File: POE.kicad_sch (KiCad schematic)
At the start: 36 parts, among them J3 7466003R, J5 7466003R, Q1 FDS2582, T1 PA2369NL, U13 VO615A, U14 TL431PK, U3 NCP1081

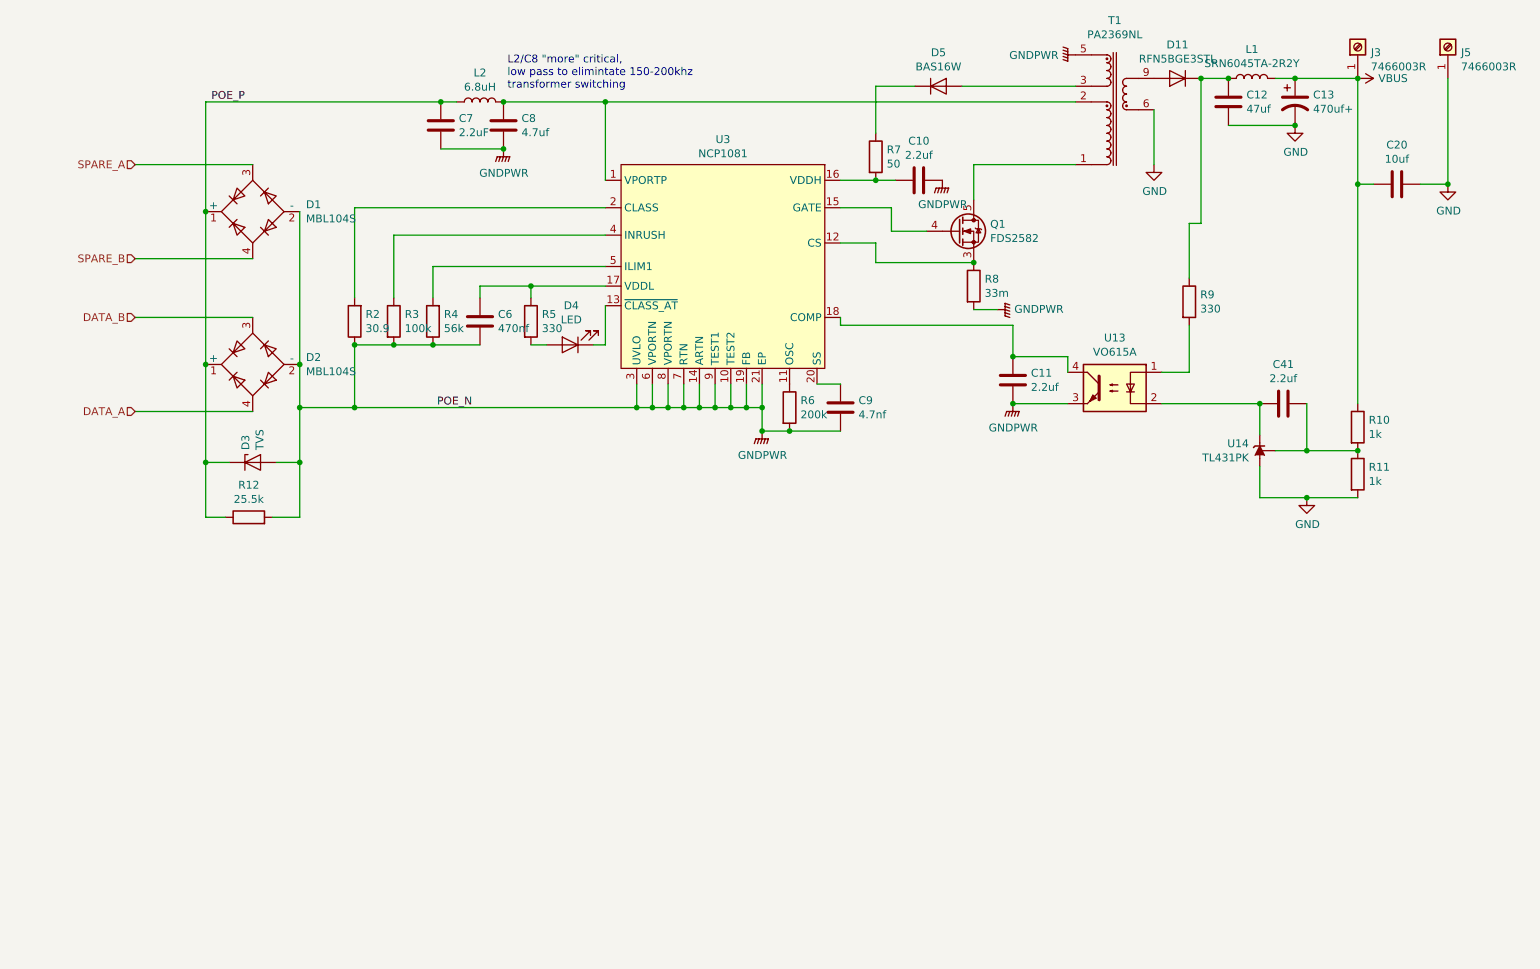
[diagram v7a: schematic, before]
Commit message: Swap low voltage caps, remove hv side LC filter
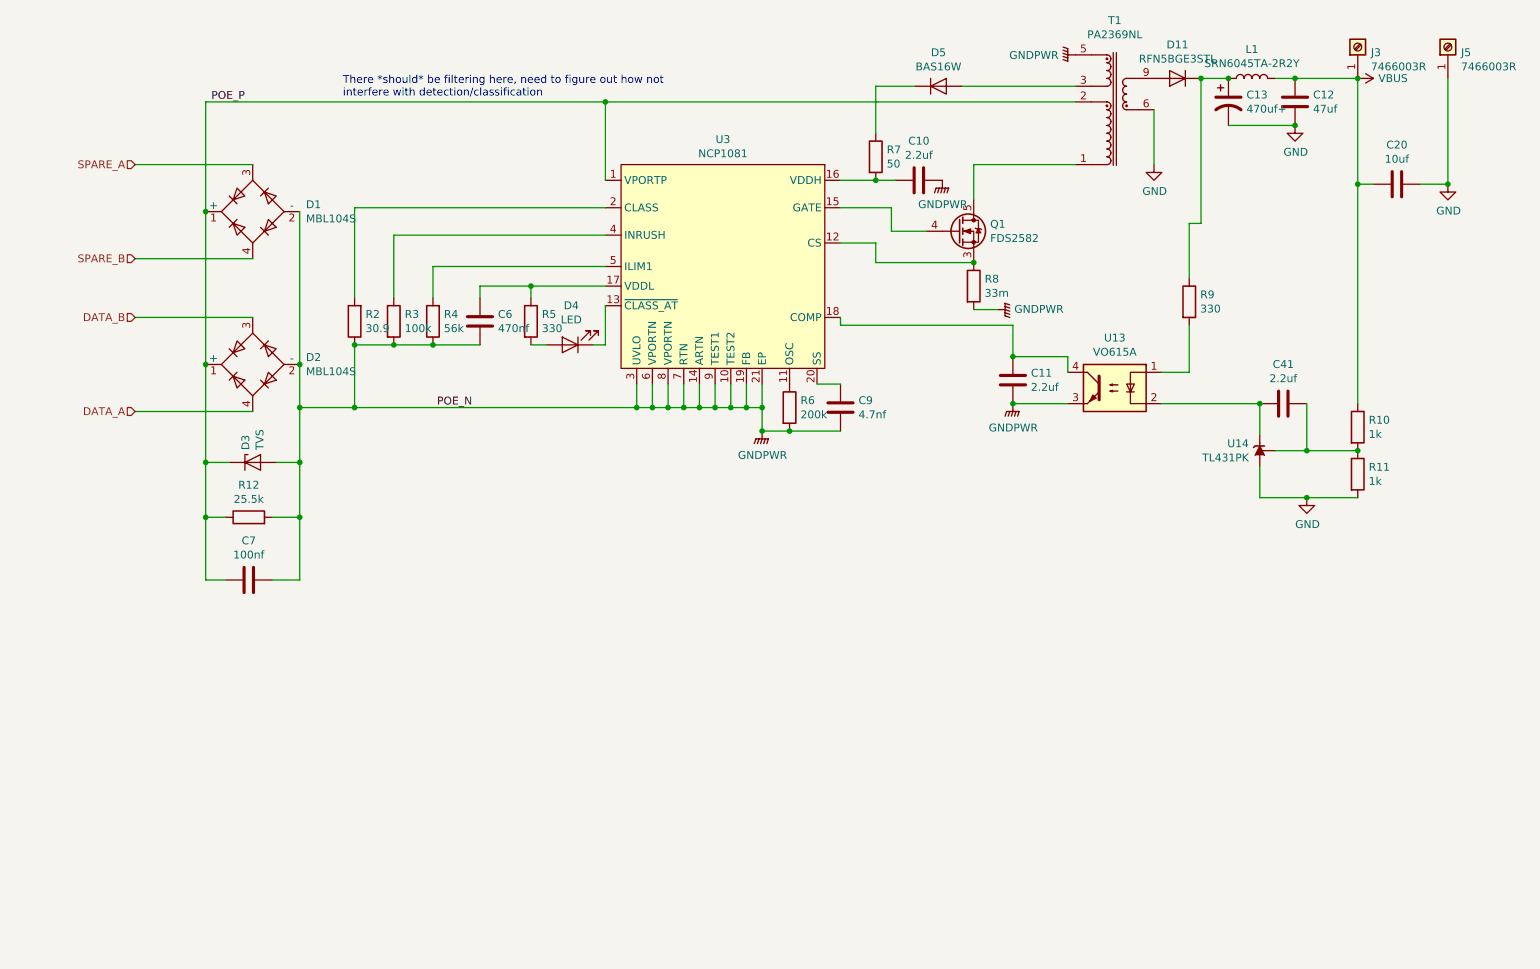
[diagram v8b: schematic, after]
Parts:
- removed C8: 4.7uf, Capacitor_SMD:C_1210_3225Metric, symbol Device:C
- removed L2: 6.8uH, Inductor_SMD:L_Bourns-SRN8040_8x8.15mm, symbol Device:L
- C7: value 2.2uF -> 100nf; footprint Capacitor_SMD:C_1210_3225Metric -> Capacitor_SMD:C_0805_2012Metric
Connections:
- net POE_P: now also T1.2, U3.1 (VPORTP)
- net VBUS: now also C12.1; no longer C13.1
- net at D11.2 (K), L1.1, R9.1: now also C13.1; no longer C12.1
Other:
- note added: "There *should* be filtering here, need to figure out how not interfere with detection/classification"
- note removed: "L2/C8 "more" critical, low pass to elimintate 150-200khz transformer switching"
- moved on the sheet: C12, C13
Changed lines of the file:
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@@
-(kicad_sch (version 20200618) (host eeschema "5.99.0-unknown-19b7755~101~ubuntu20.04.1")
+(kicad_sch (version 20200618) (host eeschema "5.99.0-unknown-af8f05d~101~ubuntu20.04.1")
   (page 4 7)
   (paper "A4")
@@
   (junction (at 52.07 86.36) (diameter 0) (color 0 0 0 0))
   (junction (at 52.07 102.235) (diameter 0) (color 0 0 0 0))
+  (junction (at 52.07 111.125) (diameter 0) (color 0 0 0 0))
   (junction (at 67.31 86.36) (diameter 0) (color 0 0 0 0))
   (junction (at 67.31 93.345) (diameter 0) (color 0 0 0 0))
   (junction (at 67.31 102.235) (diameter 0) (color 0 0 0 0))
+  (junction (at 67.31 111.125) (diameter 0) (color 0 0 0 0))
   (junction (at 76.2 83.185) (diameter 0) (color 0 0 0 0))
   (junction (at 76.2 93.345) (diameter 0) (color 0 0 0 0))
   (junction (at 82.55 83.185) (diameter 0) (color 0 0 0 0))
   (junction (at 88.9 83.185) (diameter 0) (color 0 0 0 0))
-  (junction (at 90.17 43.815) (diameter 0) (color 0 0 0 0))
-  (junction (at 100.33 43.815) (diameter 0) (color 0 0 0 0))
-  (junction (at 100.33 51.435) (diameter 0) (color 0 0 0 0))
   (junction (at 104.775 73.66) (diameter 0) (color 0 0 0 0))
   (junction (at 116.84 43.815) (diameter 0) (color 0 0 0 0))
@@
     (stroke (width 0) (type solid) (color 0 0 0 0))
   )
-  (wire (pts (xy 52.07 43.815) (xy 90.17 43.815))
+  (wire (pts (xy 52.07 43.815) (xy 116.84 43.815))
     (stroke (width 0) (type solid) (color 0 0 0 0))
   )
@@
     (stroke (width 0) (type solid) (color 0 0 0 0))
   )
+  (wire (pts (xy 52.07 111.125) (xy 52.07 121.285))
+    (stroke (width 0) (type solid) (color 0 0 0 0))
+  )
   (wire (pts (xy 52.07 111.125) (xy 55.245 111.125))
     (stroke (width 0) (type solid) (color 0 0 0 0))
   )
+  (wire (pts (xy 52.07 121.285) (xy 55.245 121.285))
+    (stroke (width 0) (type solid) (color 0 0 0 0))
+  )
   (wire (pts (xy 62.865 111.125) (xy 67.31 111.125))
     (stroke (width 0) (type solid) (color 0 0 0 0))
   )
+  (wire (pts (xy 62.865 121.285) (xy 67.31 121.285))
+    (stroke (width 0) (type solid) (color 0 0 0 0))
+  )
   (wire (pts (xy 67.31 61.595) (xy 67.31 86.36))
     (stroke (width 0) (type solid) (color 0 0 0 0))
@@
     (stroke (width 0) (type solid) (color 0 0 0 0))
   )
+  (wire (pts (xy 67.31 121.285) (xy 67.31 111.125))
+    (stroke (width 0) (type solid) (color 0 0 0 0))
+  )
   (wire (pts (xy 76.2 60.96) (xy 76.2 75.565))
     (stroke (width 0) (type solid) (color 0 0 0 0))
@@
     (stroke (width 0) (type solid) (color 0 0 0 0))
   )
-  (wire (pts (xy 90.17 43.815) (xy 92.71 43.815))
-    (stroke (width 0) (type solid) (color 0 0 0 0))
-  )
-  (wire (pts (xy 90.17 51.435) (xy 100.33 51.435))
-    (stroke (width 0) (type solid) (color 0 0 0 0))
-  )
   (wire (pts (xy 96.52 73.66) (xy 104.775 73.66))
     (stroke (width 0) (type solid) (color 0 0 0 0))
@@
     (stroke (width 0) (type solid) (color 0 0 0 0))
   )
-  (wire (pts (xy 100.33 43.815) (xy 116.84 43.815))
-    (stroke (width 0) (type solid) (color 0 0 0 0))
-  )
   (wire (pts (xy 104.775 73.66) (xy 104.775 75.565))
     (stroke (width 0) (type solid) (color 0 0 0 0))
@@
     (stroke (width 0) (type solid) (color 0 0 0 0))
   )
-  (text "L2/C8 \"more\" critical,\nlow pass to elimintate 150-200khz\ntransformer switching"
-    (at 100.965 41.91 0)
+  (text "There *should* be filtering here, need to figure out how not\ninterfere with detection/classification"
+    (at 74.295 43.18 0)
     (effects (font (size 1.27 1.27)) (justify left bottom))
   )
@@
     )
   )
-  (symbol (lib_id "power:GNDPWR") (at 100.33 51.435 0) (unit 1)
-    (in_bom yes) (on_board yes)
-    (property "Reference" "#PWR0113" (id 0) (at 100.33 56.515 0)
-      (effects (font (size 1.27 1.27)) hide)
-    )
-    (property "Value" "GNDPWR" (id 1) (at 100.3935 55.353 0))
-    (property "Footprint" "" (id 2) (at 100.33 52.705 0)
-      (effects (font (size 1.27 1.27)) hide)
-    )
-    (property "Datasheet" "" (id 3) (at 100.33 52.705 0)
-      (effects (font (size 1.27 1.27)) hide)
-    )
-  )
   (symbol (lib_id "power:GNDPWR") (at 142.24 97.155 0) (unit 1)
     (in_bom yes) (on_board yes)
@@
     )
     (property "Datasheet" "" (id 3) (at 191.77 36.195 0)
-      (effects (font (size 1.27 1.27)) hide)
-    )
-  )
-  (symbol (lib_id "Device:L") (at 96.52 43.815 90) (unit 1)
-    (in_bom yes) (on_board yes)
-    (property "Reference" "L2" (id 0) (at 96.52 39.0968 90))
-    (property "Value" "6.8uH" (id 1) (at 96.52 41.3955 90))
-    (property "Footprint" "Inductor_SMD:L_Bourns-SRN8040_8x8.15mm" (id 2) (at 96.52 43.815 0)
-      (effects (font (size 1.27 1.27)) hide)
-    )
-    (property "Datasheet" "~" (id 3) (at 96.52 43.815 0)
       (effects (font (size 1.27 1.27)) hide)
     )
@@
     )
   )
-  (symbol (lib_name "Device:C_7") (lib_id "Device:C") (at 90.17 47.625 0) (unit 1)
-    (in_bom yes) (on_board yes)
-    (property "Reference" "C7" (id 0) (at 93.0911 46.4756 0)
-      (effects (font (size 1.27 1.27)) (justify left))
-    )
-    (property "Value" "2.2uF" (id 1) (at 93.0911 48.7743 0)
-      (effects (font (size 1.27 1.27)) (justify left))
-    )
-    (property "Footprint" "Capacitor_SMD:C_1210_3225Metric" (id 2) (at 91.1352 51.435 0)
-      (effects (font (size 1.27 1.27)) hide)
-    )
-    (property "Datasheet" "~" (id 3) (at 90.17 47.625 0)
+  (symbol (lib_name "Device:C_7") (lib_id "Device:C") (at 59.055 121.285 90) (unit 1)
+    (in_bom yes) (on_board yes)
+    (property "Reference" "C7" (id 0) (at 59.055 114.9158 90))
+    (property "Value" "100nf" (id 1) (at 59.055 117.2145 90))
+    (property "Footprint" "Capacitor_SMD:C_0805_2012Metric" (id 2) (at 62.865 120.3198 0)
+      (effects (font (size 1.27 1.27)) hide)
+    )
+    (property "Datasheet" "~" (id 3) (at 59.055 121.285 0)
       (effects (font (size 1.27 1.27)) hide)
     )
@@
     )
     (property "Datasheet" "~" (id 3) (at 96.52 79.375 0)
-      (effects (font (size 1.27 1.27)) hide)
-    )
-  )
-  (symbol (lib_name "Device:C_8") (lib_id "Device:C") (at 100.33 47.625 0) (unit 1)
-    (in_bom yes) (on_board yes)
-    (property "Reference" "C8" (id 0) (at 103.2511 46.4756 0)
-      (effects (font (size 1.27 1.27)) (justify left))
-    )
-    (property "Value" "4.7uf" (id 1) (at 103.251 48.774 0)
-      (effects (font (size 1.27 1.27)) (justify left))
-    )
-    (property "Footprint" "Capacitor_SMD:C_1210_3225Metric" (id 2) (at 101.2952 51.435 0)
-      (effects (font (size 1.27 1.27)) hide)
-    )
-    (property "Datasheet" "~" (id 3) (at 100.33 47.625 0)
       (effects (font (size 1.27 1.27)) hide)
     )
@@
     )
   )
-  (symbol (lib_id "Device:C") (at 217.805 43.815 0) (unit 1)
-    (in_bom yes) (on_board yes)
-    (property "Reference" "C12" (id 0) (at 220.7261 42.6656 0)
-      (effects (font (size 1.27 1.27)) (justify left))
-    )
-    (property "Value" "47uf" (id 1) (at 220.7261 44.9643 0)
-      (effects (font (size 1.27 1.27)) (justify left))
-    )
-    (property "Footprint" "Capacitor_SMD:C_0805_2012Metric" (id 2) (at 218.7702 47.625 0)
+  (symbol (lib_id "Device:CP1") (at 217.805 43.815 0) (unit 1)
+    (in_bom yes) (on_board yes)
+    (property "Reference" "C13" (id 0) (at 220.7261 42.6656 0)
+      (effects (font (size 1.27 1.27)) (justify left))
+    )
+    (property "Value" "470uf+" (id 1) (at 220.7261 44.9643 0)
+      (effects (font (size 1.27 1.27)) (justify left))
+    )
+    (property "Footprint" "Capacitor_SMD:CP_Elec_8x10" (id 2) (at 217.805 43.815 0)
       (effects (font (size 1.27 1.27)) hide)
     )
@@
     )
   )
-  (symbol (lib_id "Device:CP1") (at 228.6 43.815 0) (unit 1)
-    (in_bom yes) (on_board yes)
-    (property "Reference" "C13" (id 0) (at 231.5211 42.6656 0)
-      (effects (font (size 1.27 1.27)) (justify left))
-    )
-    (property "Value" "470uf+" (id 1) (at 231.5211 44.9643 0)
-      (effects (font (size 1.27 1.27)) (justify left))
-    )
-    (property "Footprint" "Capacitor_SMD:CP_Elec_8x10" (id 2) (at 228.6 43.815 0)
-      (effects (font (size 1.27 1.27)) hide)
-    )
+  (symbol (lib_id "Device:C") (at 228.6 43.815 0) (unit 1)
+    (in_bom yes) (on_board yes)
+    (property "Reference" "C12" (id 0) (at 231.5211 42.6656 0)
+      (effects (font (size 1.27 1.27)) (justify left))
+    )
+    (property "Value" "47uf" (id 1) (at 231.5211 44.9643 0)
+      (effects (font (size 1.27 1.27)) (justify left))
+    )
+    (property "Footprint" "Capacitor_SMD:C_0805_2012Metric" (id 2) (at 229.5652 47.625 0)
+      (effects (font (size 1.27 1.27)) hide)
+    )
